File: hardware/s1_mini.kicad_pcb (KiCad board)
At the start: 2 copper layers, 31 x 54.4 mm, 12 parts, among them P1 USB_Edge, U1 AP2114H, U2 SM220UF1, U3 Wemos_D1_Mini

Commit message: Clean up part placements.
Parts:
- moved R6 13.8 mm to (142.2, 115.6)
- moved R5 10.2 mm to (156.2, 115.6)
- moved U1 1.40 mm to (149.2, 120.0)
- moved R1 0.63 mm to (142.2, 95.2)
- moved R2 0.63 mm to (154.9, 97.8)
- moved R3 0.63 mm to (142.2, 97.8)
- moved R4 0.63 mm to (154.9, 95.2)
- moved C2 0.57 mm to (142.2, 118.1)
- moved C1 0.36 mm to (156.2, 118.1)

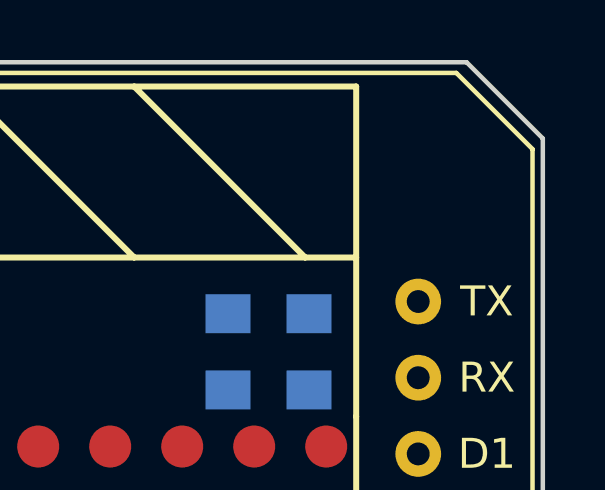
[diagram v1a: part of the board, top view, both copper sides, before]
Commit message: Add power LED.
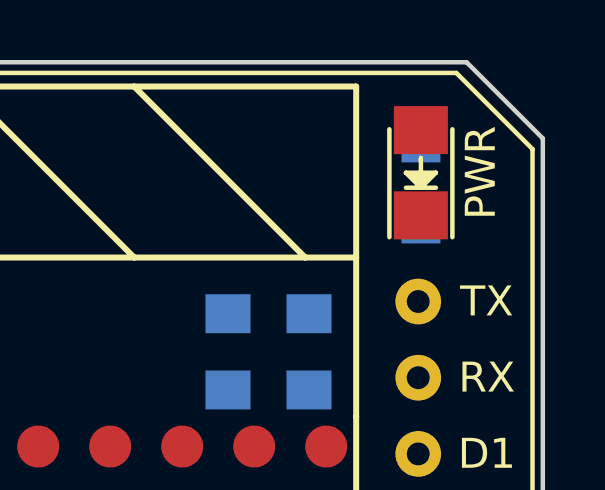
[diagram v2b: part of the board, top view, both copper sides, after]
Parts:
- added D1: PWR, LEDs:LED_1206, F.Cu at (160.0, 90.6)
- added R7: 10K, Resistors_SMD:R_0805_HandSoldering, B.Cu at (160.0, 90.8)
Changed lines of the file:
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@@
 (kicad_pcb (version 4) (host pcbnew 4.0.3-stable)
   (general
-    (links 41)
-    (no_connects 41)
+    (links 44)
+    (no_connects 44)
     (area 133.020999 86.792999 164.159001 141.299001)
     (thickness 1.6)
@@
     (tracks 0)
     (zones 0)
-    (modules 12)
-    (nets 43)
+    (modules 14)
+    (nets 44)
   )
   (page A4)
@@
     (pad_to_mask_clearance 0.2)
     (aux_axis_origin 0 0)
-    (visible_elements FFFFFF7F)
+    (visible_elements 7FFFFFFF)
     (pcbplotparams
       (layerselection 0x00030_80000001)
@@
   (net 41 "Net-(U2-PadA7)")
   (net 42 "Net-(U2-PadB7)")
+  (net 43 "Net-(D1-Pad2)")
   (net_class Default "This is the default net class."
     (clearance 0.2)
@@
     (add_net GND)
     (add_net "Net-(C2-Pad1)")
+    (add_net "Net-(D1-Pad2)")
     (add_net "Net-(P1-Pad2)")
     (add_net "Net-(P1-Pad3)")
@@
       (net 2 GND))
   )
+  (module LEDs:LED_1206 (layer F.Cu)
+    (at 160.02 90.551 90)
+    (descr "LED 1206 smd package")
+    (tags "LED1206 SMD")
+    (attr smd)
+    (fp_text reference D1 (at 0 -2 90) (layer F.SilkS) hide
+      (effects (font (size 1 1) (thickness 0.15)))
+    )
+    (fp_text value PWR (at 0 2 90) (layer F.SilkS)
+      (effects (font (size 1 1) (thickness 0.15)))
+    )
+    (fp_line (start -0.5 -0.5) (end -0.5 0.5) (layer F.Fab) (width 0.15))
+    (fp_line (start -0.5 0) (end 0 -0.5) (layer F.Fab) (width 0.15))
+    (fp_line (start 0 0.5) (end -0.5 0) (layer F.Fab) (width 0.15))
+    (fp_line (start 0 -0.5) (end 0 0.5) (layer F.Fab) (width 0.15))
+    (fp_line (start -1.6 0.8) (end -1.6 -0.8) (layer F.Fab) (width 0.15))
+    (fp_line (start 1.6 0.8) (end -1.6 0.8) (layer F.Fab) (width 0.15))
+    (fp_line (start 1.6 -0.8) (end 1.6 0.8) (layer F.Fab) (width 0.15))
+    (fp_line (start -1.6 -0.8) (end 1.6 -0.8) (layer F.Fab) (width 0.15))
+    (fp_line (start -2.15 1.05) (end 1.45 1.05) (layer F.SilkS) (width 0.15))
+    (fp_line (start -2.15 -1.05) (end 1.45 -1.05) (layer F.SilkS) (width 0.15))
+    (fp_line (start -0.1 -0.3) (end -0.1 0.3) (layer F.SilkS) (width 0.15))
+    (fp_line (start -0.1 0.3) (end -0.4 0) (layer F.SilkS) (width 0.15))
+    (fp_line (start -0.4 0) (end -0.2 -0.2) (layer F.SilkS) (width 0.15))
+    (fp_line (start -0.2 -0.2) (end -0.2 0.05) (layer F.SilkS) (width 0.15))
+    (fp_line (start -0.2 0.05) (end -0.25 0) (layer F.SilkS) (width 0.15))
+    (fp_line (start -0.5 -0.5) (end -0.5 0.5) (layer F.SilkS) (width 0.15))
+    (fp_line (start 0 0) (end 0.5 0) (layer F.SilkS) (width 0.15))
+    (fp_line (start -0.5 0) (end 0 -0.5) (layer F.SilkS) (width 0.15))
+    (fp_line (start 0 -0.5) (end 0 0.5) (layer F.SilkS) (width 0.15))
+    (fp_line (start 0 0.5) (end -0.5 0) (layer F.SilkS) (width 0.15))
+    (fp_line (start 2.5 -1.25) (end -2.5 -1.25) (layer F.CrtYd) (width 0.05))
+    (fp_line (start -2.5 -1.25) (end -2.5 1.25) (layer F.CrtYd) (width 0.05))
+    (fp_line (start -2.5 1.25) (end 2.5 1.25) (layer F.CrtYd) (width 0.05))
+    (fp_line (start 2.5 1.25) (end 2.5 -1.25) (layer F.CrtYd) (width 0.05))
+    (pad 2 smd rect (at 1.41986 0 270) (size 1.59766 1.80086) (layers F.Cu F.Paste F.Mask)
+      (net 43 "Net-(D1-Pad2)"))
+    (pad 1 smd rect (at -1.41986 0 270) (size 1.59766 1.80086) (layers F.Cu F.Paste F.Mask)
+      (net 2 GND))
+    (model LEDs.3dshapes/LED_1206.wrl
+      (at (xyz 0 0 0))
+      (scale (xyz 1 1 1))
+      (rotate (xyz 0 0 180))
+    )
+  )
+  (module Resistors_SMD:R_0805_HandSoldering (layer B.Cu)
+    (at 160.02 90.805 90)
+    (descr "Resistor SMD 0805, hand soldering")
+    (tags "resistor 0805")
+    (attr smd)
+    (fp_text reference R7 (at 0 -2.54 180) (layer B.SilkS)
+      (effects (font (size 1 1) (thickness 0.15)) (justify mirror))
+    )
+    (fp_text value 10K (at 0 -2.1 90) (layer B.Fab)
+      (effects (font (size 1 1) (thickness 0.15)) (justify mirror))
+    )
+    (fp_line (start -2.4 1) (end 2.4 1) (layer B.CrtYd) (width 0.05))
+    (fp_line (start -2.4 -1) (end 2.4 -1) (layer B.CrtYd) (width 0.05))
+    (fp_line (start -2.4 1) (end -2.4 -1) (layer B.CrtYd) (width 0.05))
+    (fp_line (start 2.4 1) (end 2.4 -1) (layer B.CrtYd) (width 0.05))
+    (fp_line (start 0.6 -0.875) (end -0.6 -0.875) (layer B.SilkS) (width 0.15))
+    (fp_line (start -0.6 0.875) (end 0.6 0.875) (layer B.SilkS) (width 0.15))
+    (pad 1 smd rect (at -1.35 0 90) (size 1.5 1.3) (layers B.Cu B.Paste B.Mask)
+      (net 43 "Net-(D1-Pad2)"))
+    (pad 2 smd rect (at 1.35 0 90) (size 1.5 1.3) (layers B.Cu B.Paste B.Mask)
+      (net 3 "Net-(C2-Pad1)"))
+    (model Resistors_SMD.3dshapes/R_0805_HandSoldering.wrl
+      (at (xyz 0 0 0))
+      (scale (xyz 1 1 1))
+      (rotate (xyz 0 0 0))
+    )
+  )
   (gr_line (start 154.432 141.224) (end 154.432 127) (angle 90) (layer Edge.Cuts) (width 0.15))

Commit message: Route and finish up board.
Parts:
- added G***: LOGO, CrumpPrintSymbols:Symbol_OSHW-Logo_12.5mm_NoText_Silkscreen, B.Cu at (148.6, 104.8)
- moved R7 25.9 mm to (160.4, 116.7), turned to 270 degrees
- moved R5 17.7 mm to (139.4, 110.0), turned to 90 degrees
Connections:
- P1 pad 2: Net-(P1-Pad2) -> (no net)
- P1 pad 3: Net-(P1-Pad3) -> (no net)
- R7 pad 2: Net-(C2-Pad1) -> +3V3
- U2 pad A6: Net-(U2-PadA6) -> (no net)
- U2 pad A7: Net-(U2-PadA7) -> (no net)
- U2 pad B2: Net-(U2-PadB2) -> (no net)
- U2 pad B6: Net-(U2-PadB6) -> (no net)
- U2 pad B7: Net-(U2-PadB7) -> (no net)
- U2 pad C4: Net-(U2-PadC4) -> (no net)
- U2 pad C5: Net-(U2-PadC5) -> (no net)
- U2 pad D3: Net-(U2-PadD3) -> (no net)
- U2 pad E1: Net-(U2-PadE1) -> (no net)
- U2 pad E2: Net-(U2-PadE2) -> (no net)
- U2 pad E3: Net-(U2-PadE3) -> (no net)
- U2 pad F1: Net-(U2-PadF1) -> (no net)
- U2 pad F2: Net-(U2-PadF2) -> (no net)
- U2 pad F3: Net-(U2-PadF3) -> (no net)
- U2 pad F4: Net-(U2-PadF4) -> (no net)
- U2 pad G1: Net-(U2-PadG1) -> (no net)
- U2 pad G2: Net-(U2-PadG2) -> (no net)
- U2 pad G3: Net-(U2-PadG3) -> (no net)
- U2 pad G5: Net-(U2-PadG5) -> (no net)
- U2 pad H2: Net-(U2-PadH2) -> (no net)
- U2 pad H3: Net-(U2-PadH3) -> (no net)
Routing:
- net GND: track 0.00 -> 48.2 mm, vias 0 -> 9
- net +3V3: track 0.00 -> 41.9 mm, vias 0 -> 5
- net +5V: track 0.00 -> 40.1 mm, vias 0 -> 1
- net SNAP_TXD1: track 0.00 -> 29.5 mm, vias 0 -> 2
- net SNAP_RXD0_INT: track 0.00 -> 28.8 mm, vias 0 -> 2
- net SNAP_ADC0: track 0.00 -> 28.3 mm, vias 0 -> 2
- net SNAP_SPI_MISO: track 0.00 -> 28.1 mm, vias 0 -> 2
- net Net-(D1-Pad2): track 0.00 -> 28.0 mm, vias 0 -> 1
- net SNAP_RXD1: track 0.00 -> 27.5 mm, vias 0 -> 1
- net SNAP_TXD0: track 0.00 -> 26.7 mm, vias 0 -> 1
- net SNAP_PB5_PWM_INT: track 0.00 -> 26.2 mm, vias 0 -> 2
- net D1_RX: track 0.00 -> 23.7 mm, vias 0 -> 1
- net SNAP_SPI_CLK: track 0.00 -> 22.2 mm, vias 0 -> 2
- net SNAP_PB6_PWM_INT: track 0.00 -> 21.2 mm, vias 0 -> 1
- net SNAP_SPI_MOSI: track 0.00 -> 18.3 mm, vias 0 -> 2
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- added copper zone on F.Cu, net +3V3
- added copper zone on B.Cu, net GND
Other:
- board text added: "@tylercrumpton"
- board text added: "CC-BY-SA 4.0"
- board text added: "S1 Mini"
- board text added: "v1.0"
